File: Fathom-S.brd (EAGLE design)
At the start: 112.4 x 45.7 mm, 114 parts, among them IC1 LMH6643, IC2 LMH6643, IC3 ST490AB, IC4 ST490AB, IC5 FT230XS, Q1 BC817-40W, U1 MC7812, U2 MC7805, U4 INA139, U5 MC7805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

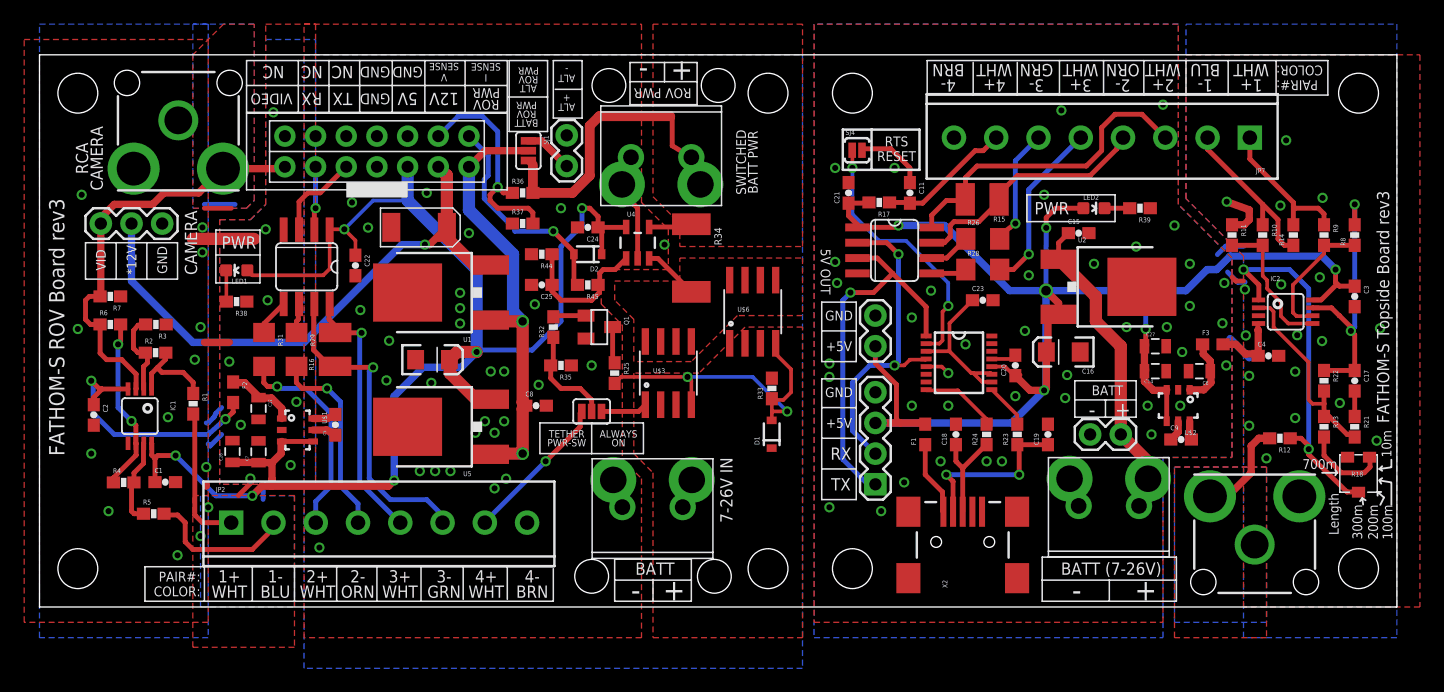
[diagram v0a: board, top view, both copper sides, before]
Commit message: Fixed a few more layout issues and connected the pot wiper to open end for safety.
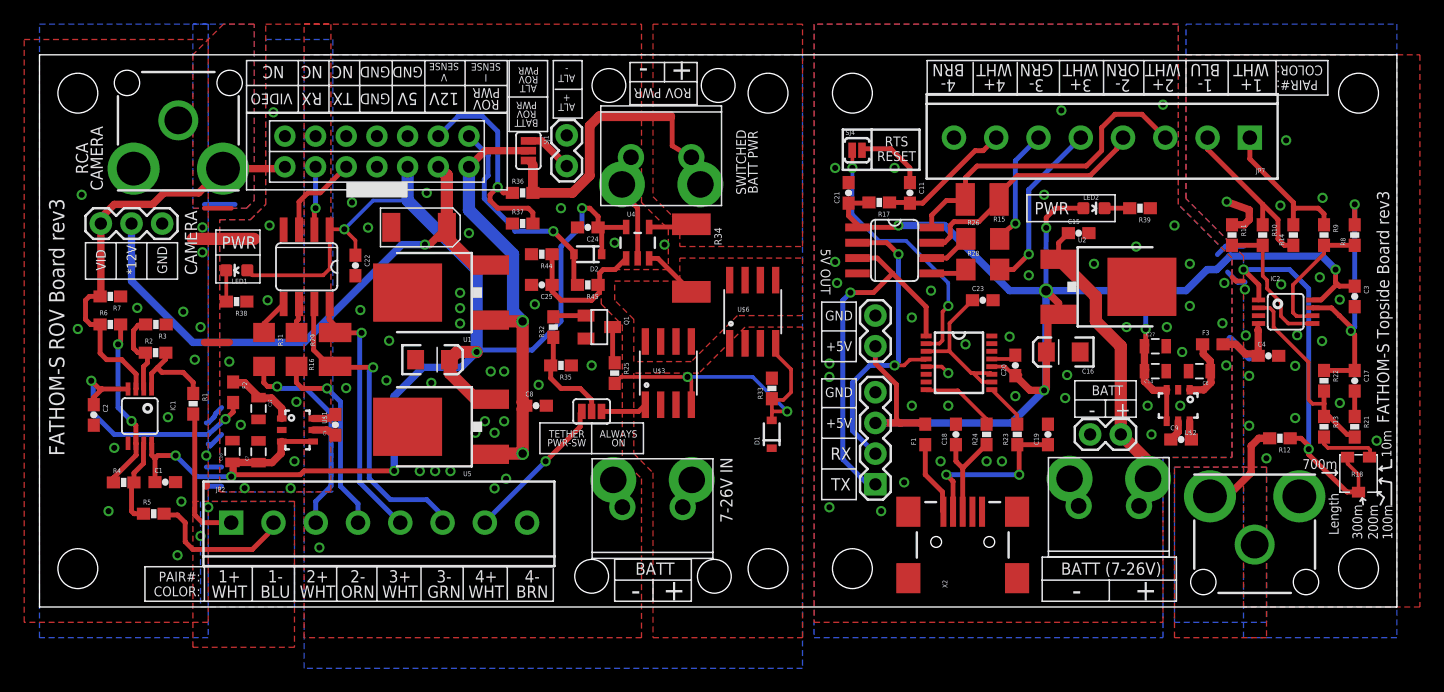
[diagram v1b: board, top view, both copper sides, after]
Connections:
- net N$17: now also R18.3
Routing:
- net N$17: track 30.3 -> 33.6 mm
- net VCC-ISO: track 121.8 -> 119.1 mm
- net N$12: track 6.96 -> 5.28 mm
- net GND-ISO: track 23.2 -> 22.6 mm, vias 49 -> 55

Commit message: Moved components slightly to move pot up.
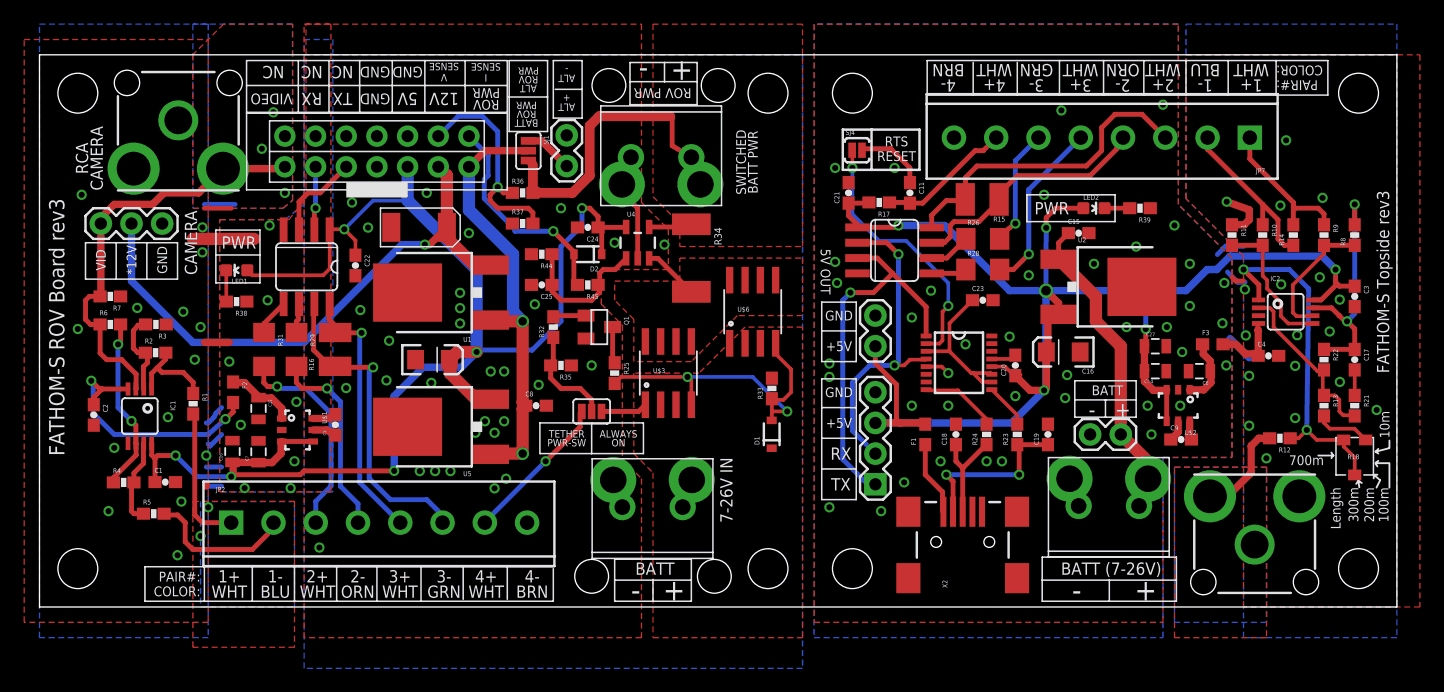
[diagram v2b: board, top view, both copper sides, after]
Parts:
- moved C17 1.75 mm to (108.9, 20.5)
- moved R13 1.75 mm to (106.4, 16.7)
- moved R21 1.75 mm to (108.9, 16.7)
- moved R22 1.75 mm to (106.4, 20.5)
- moved R18 1.46 mm to (108.9, 12.4)
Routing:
- net N$17: track 33.6 -> 29.4 mm
- net N$15: track 16.8 -> 14.3 mm
- net N$14: track 22.4 -> 20.1 mm
- net GND-ISO: vias 55 -> 57
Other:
- board text added: "FATHOM-S Topside rev3"
- board text removed: "FATHOM-S Topside Board rev3"
